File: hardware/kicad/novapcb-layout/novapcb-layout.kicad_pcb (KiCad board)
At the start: 4 copper layers, 36 x 36 mm, 70 parts, among them J1 USB-C_2.0, J10 CRSF_solder_pad, J11 ESC_solder_pad, J12 ESC_solder_pad, J13 ESC_solder_pad, J14 ESC_solder_pad, J15 ESC_solder_pad, J16 ESC_solder_pad, J17 ESC_solder_pad, J18 ESC_solder_pad, J2 microSD_DM3AT, J3 TELEM_6P, J4 MAUCH_6P, J5 GPS_MAG_10P, J9 SWD_10P, U1 STM32H743VITx, U2 AP2112K-3.3, U3 ICM-42688-P, U4 DPS310, U5 USBLC6-2P6, Y1 8MHz

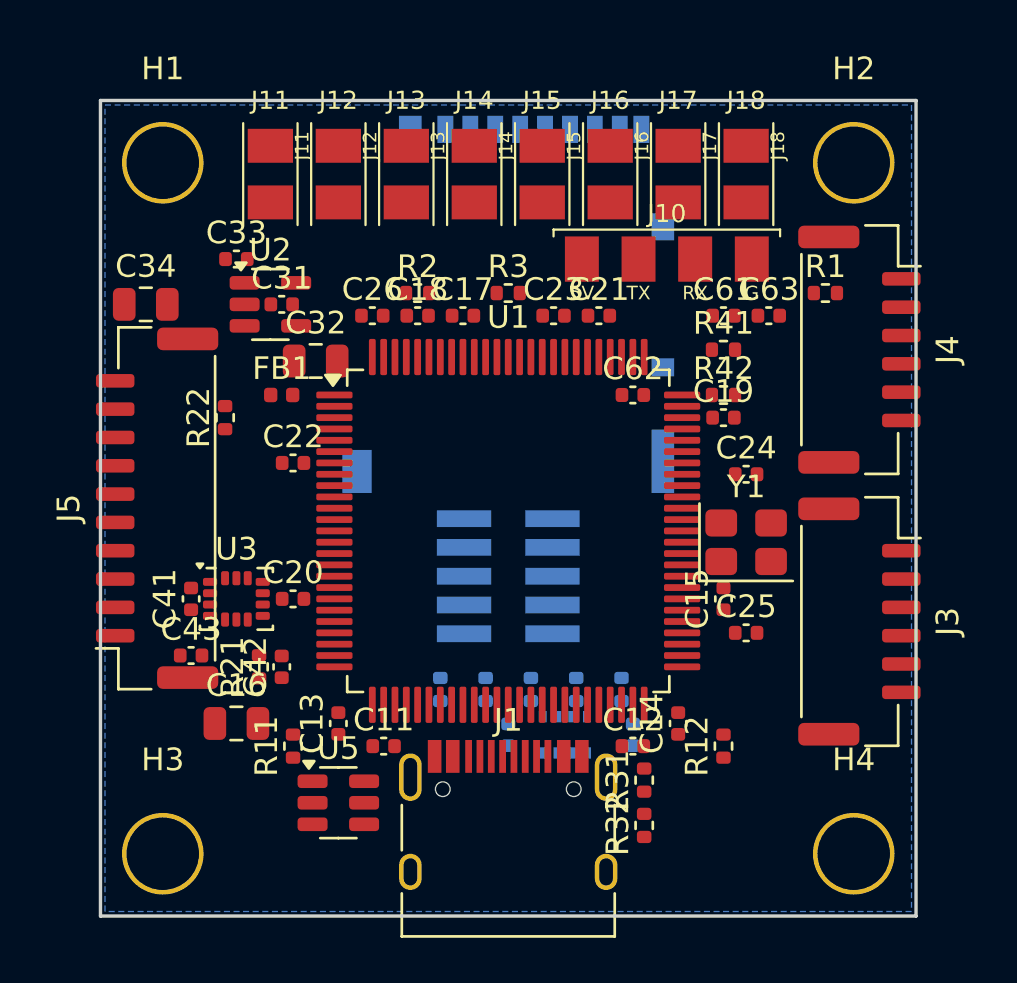
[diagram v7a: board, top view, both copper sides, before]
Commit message: Phase 4e: Freerouting autoroute pass — bulk-ok-critical-poor result
Per master 4e dispatch: ran Freerouting on the real placed-and-planed
board (vs P0 scatter test). Result classified per the freerouting-result
fork; scoped GUI residual identified.

## Falsifiable prediction vs actual

PREDICTED (committed pre-run):
- 75-85% completion (~5-10 nets incomplete)
- Outcome class: bulk-ok-critical-poor with USB diff pair likely scoped
  GUI residual
- DRC: 0 errors on routed traces likely

ACTUAL:
- Freerouting score: 96.1% by connection count (7/181 unrouted) — BETTER
  than connection-count prediction
- BUT by net-count: 17 signal nets have ≥1 unconnected pad — exceeds
  the 5% gate (34% of ~50 signal nets)
- Outcome class: **bulk-ok-critical-poor** ✓ predicted correctly
- DRC initial: 112 drill_out_of_range (Freerouting used 0.25mm drill;
  board's min_through_hole_diameter was 0.3mm). Fixed by lowering rule
  to 0.25mm (matches netclass via_drill; JLCPCB 4-layer free spec drill
  min 0.20mm; 0.25mm comfortable margin). Post-fix: **0 DRC errors**.

## Run stats

- Freerouting v2.2.4 invoked headless: java -jar ... -mt 4 -mp 50
- Wall clock: 5.0 min (vs P0 estimate 30-60 min — much faster than
  expected, because the real board is more routable than the scatter
  scale-test)
- 26 passes auto-router; final score 976.34
- Imported 771 tracks (459 F.Cu + 121 B.Cu + ~191 zone/etc.) + 153 vias
- DSN/SES round-trip clean (Freerouting via P0 toolchain)

## Scoped GUI residual — 17 nets

Excluding plane-served nets + testpoints (single-pad expected), the
17 nets with incomplete connections are:

| Net | Unconnected pads | Notes |
|---|---:|---|
| HSE_OUT | 3 | Crystal Y1 east side; tight area |
| SDMMC1_D2 | 3 | SDMMC family, B.Cu route + R54 pullup |
| SDMMC1_D0/D1/CMD/D3 | 2 ea | Same family, B.Cu transition + pullup |
| SDMMC1_CLK | 1 | Same family |
| MOT1/2/3 | 2 ea | ESC outputs (DShot lines) |
| USART1_RX | 2 | Telem J3 |
| USB_DP | 2 | USB diff pair partly unrouted |
|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
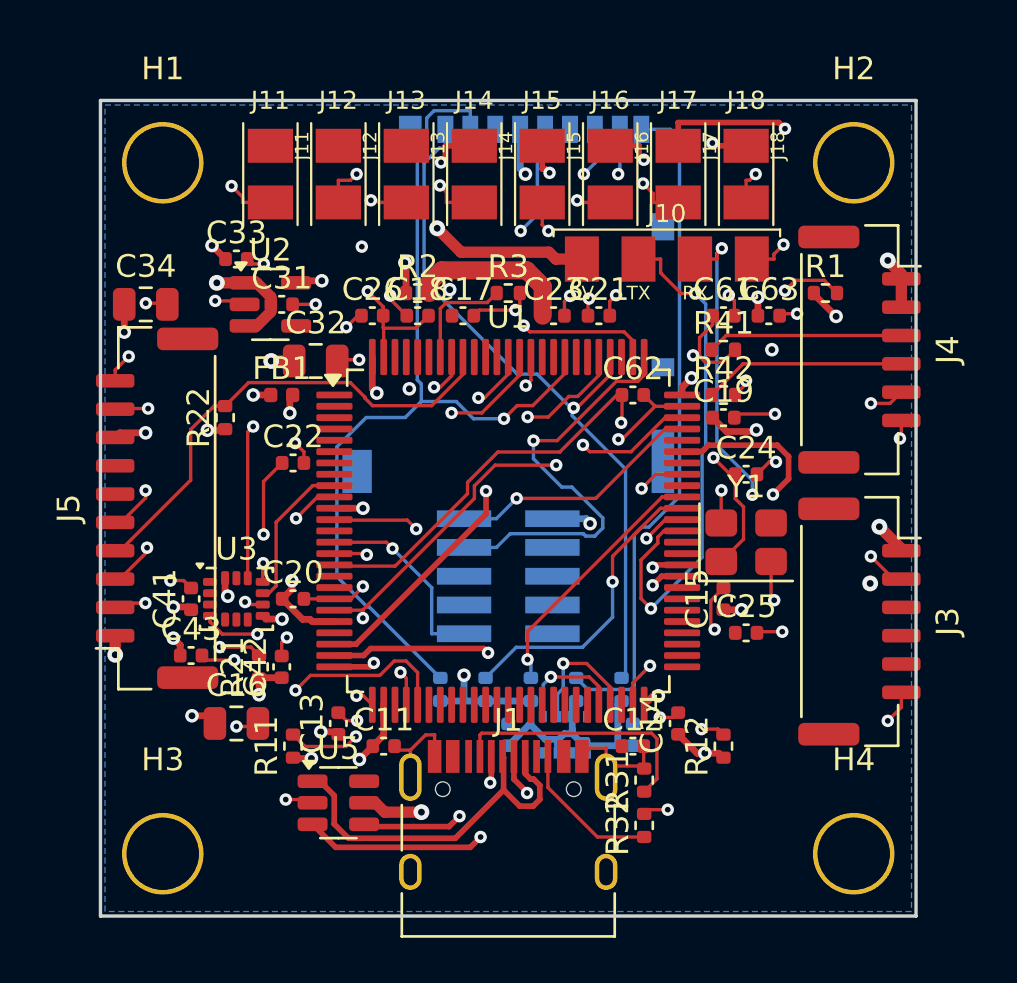
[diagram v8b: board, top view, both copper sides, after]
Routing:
- net GND: track 0.00 -> 81.5 mm, vias 0 -> 45
- net +3V3: track 0.00 -> 48.3 mm, vias 0 -> 26
- net +3V3A: track 0.00 -> 45.9 mm, vias 0 -> 7
- net SDMMC1_D0: track 0.00 -> 44.9 mm, vias 0 -> 2
- net +5V: track 0.00 -> 44.6 mm, vias 0 -> 8
- net VREF_P: track 0.00 -> 43.4 mm, vias 0 -> 5
- net MOT5: track 0.00 -> 41.1 mm, vias 0 -> 2
- net SDMMC1_CMD: track 0.00 -> 40.6 mm, vias 0 -> 1
- net MOT6: track 0.00 -> 38.0 mm, vias 0 -> 3
- net SDMMC1_D1: track 0.00 -> 36.5 mm, vias 0 -> 2
- net I2C1_SDA: track 0.00 -> 35.4 mm, vias 0 -> 3
- net SDMMC1_D3: track 0.00 -> 32.1 mm, vias 0 -> 1
- net USB_DM: track 0.00 -> 31.8 mm, vias 0 -> 2
- net MOT7: track 0.00 -> 30.8 mm, vias 0 -> 2
- net SDMMC1_D2: track 0.00 -> 29.9 mm
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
